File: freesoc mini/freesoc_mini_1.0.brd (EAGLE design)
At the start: 50.8 x 17.8 mm, 50 parts, among them IC1 CY7C68013A-56QFNLFXC, IC2 24LC00OT, Y1 XRCGB24M000F0L00R0

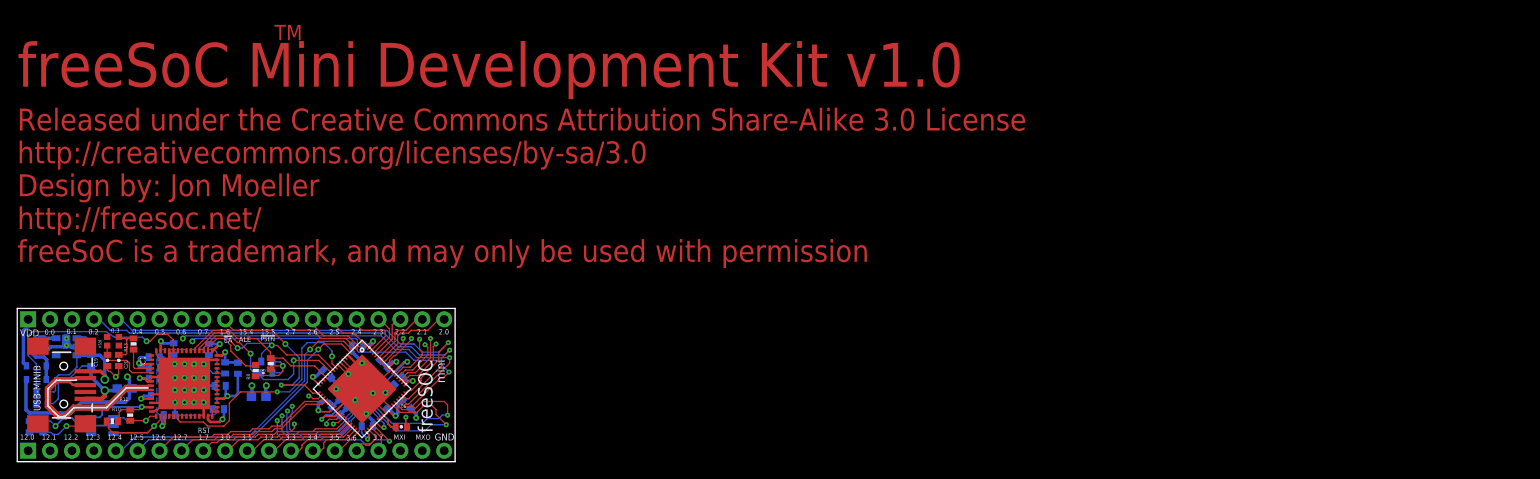
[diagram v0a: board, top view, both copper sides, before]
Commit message: DFM changes to freesoc mini board
All vias tented.

Updated land pattern for FX2 and PSoC for improved reliability and
smaller defect rate.
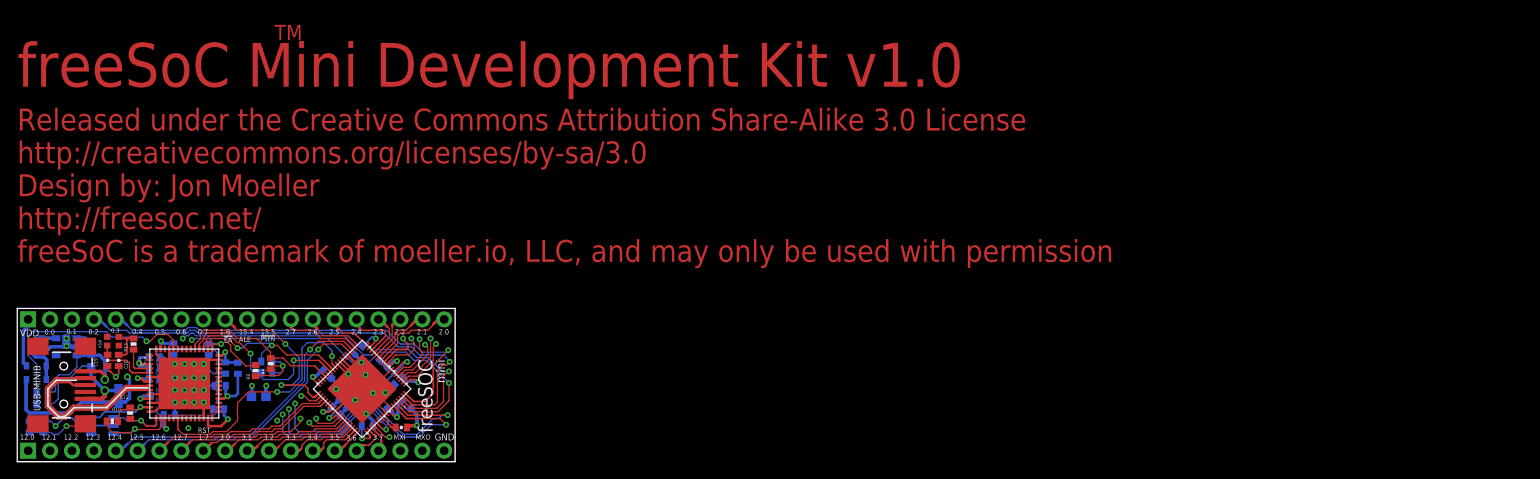
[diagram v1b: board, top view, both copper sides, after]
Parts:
- moved C16 1.13 mm to (17.1, 8.26), turned to 90 degrees
- moved C11 0.53 mm to (45.0, 13.6), turned to 315 degrees
- moved R11 0.24 mm to (18.5, 6.27)
- moved C6 0.08 mm to (50.0, 4.60)
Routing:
- net MXI: track 11.3 -> 18.3 mm
- net MXO: track 15.9 -> 19.0 mm
- net P0.1: track 54.5 -> 57.6 mm
- net P0.0: track 58.0 -> 60.4 mm
- net VCC: track 69.4 -> 71.7 mm
- net VCCD: track 17.2 -> 15.1 mm
- net GND: track 134.2 -> 136.2 mm
- net P0.2: track 51.6 -> 53.7 mm
- net SDA: track 13.3 -> 11.3 mm
- net !PSEN: track 20.2 -> 22.1 mm
- net ALE: track 24.9 -> 26.5 mm
- net !EA: track 20.1 -> 21.5 mm
- net P0.3: track 48.7 -> 50.2 mm
- net P0.7: track 32.7 -> 34.1 mm
- net RESET: track 17.8 -> 19.2 mm
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- added copper zone on layer 15, net N$6
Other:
- board text added: "freeSoC is a trademark of moeller.io, LLC, and may only be used with permission"
- board text removed: "freeSoC is a trademark, and may only be used with permission"

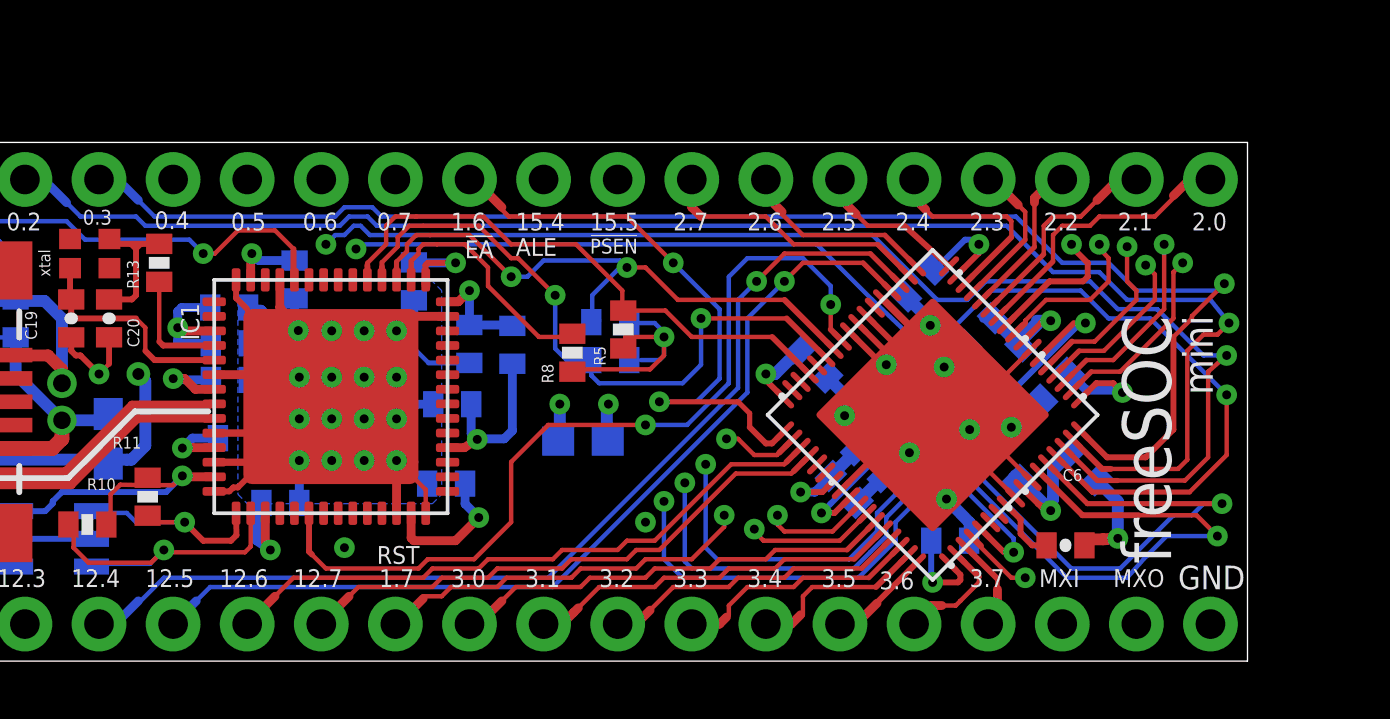
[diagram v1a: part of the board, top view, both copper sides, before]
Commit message: More DFM changes for freesoc mini
Updated FX2 QFN thermal pad to meet cypress spec.

Updated PSoC QFN thermal pad to meet cypress spec.

Added tented vias on thermal pad for both chips, proper solder paste
stencil, and removed solder mask from bottom of vias to prevent
outgassing.
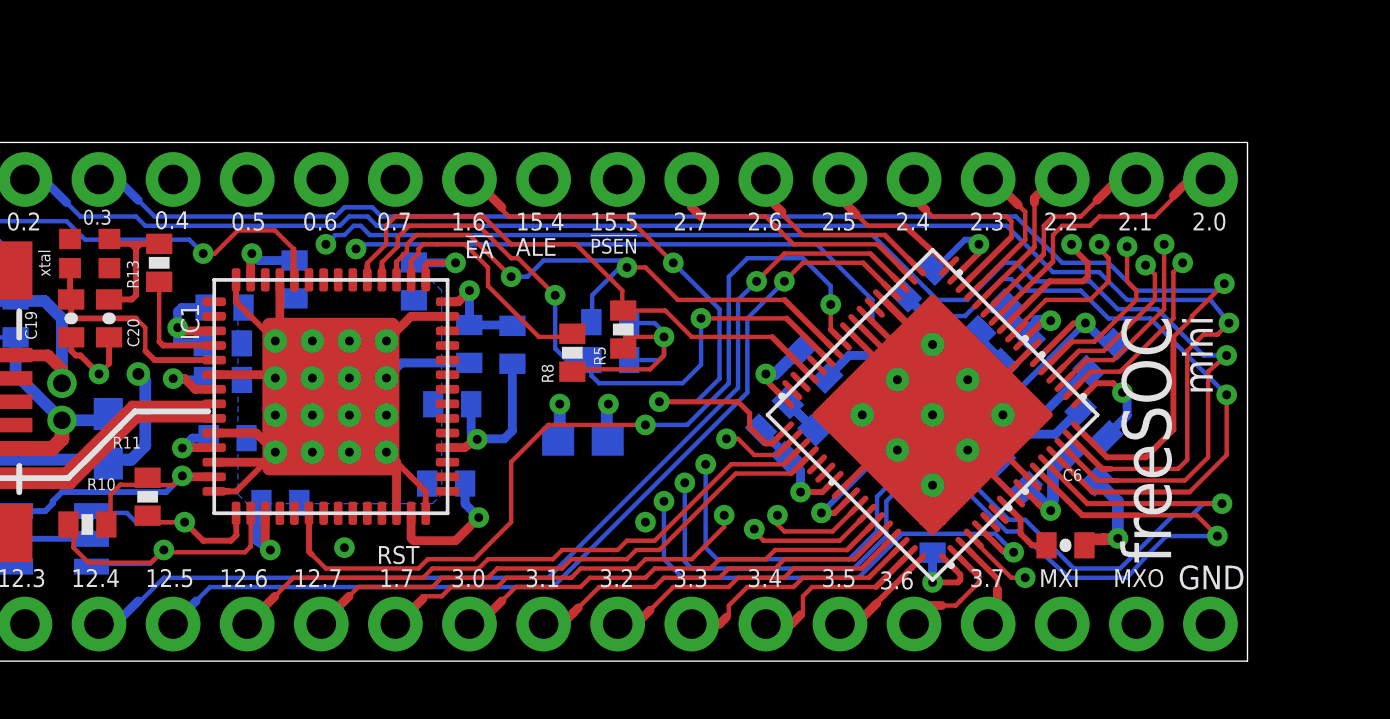
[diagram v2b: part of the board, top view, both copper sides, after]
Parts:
- moved C14 6.57 mm to (51.2, 11.0), turned to 315 degrees
- moved C7 3.64 mm to (40.0, 9.03), turned to 135 degrees
- moved C12 2.17 mm to (40.9, 8.09), turned to 135 degrees
- moved C10 1.82 mm to (50.9, 8.80), turned to 45 degrees
- moved C13 0.67 mm to (47.5, 12.4)
- moved C15 0.65 mm to (45.4, 5.00), turned to 90 degrees
- moved C5 0.45 mm to (48.3, 11.3)
- moved C4 0.40 mm to (48.2, 7.07)
- moved C26 0.32 mm to (21.2, 8.28)
- moved C21 0.24 mm to (21.1, 10.3)
- moved C3 0.24 mm to (21.1, 11.5)
- moved C2 0.16 mm to (21.1, 12.8)
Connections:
- net GND: now also IC1.P$1, IC1.P$10, IC1.P$11, IC1.P$12, IC1.P$13, IC1.P$14, IC1.P$15, IC1.P$16, IC1.P$2, IC1.P$3, IC1.P$4, IC1.P$5, IC1.P$6, IC1.P$7, IC1.P$8, IC1.P$9, U$1.P$1, U$1.P$2, U$1.P$3, U$1.P$4, U$1.P$5, U$1.P$6, U$1.P$7, U$1.P$8, U$1.P$9
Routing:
- net GND: track 136.2 -> 125.2 mm, vias 31 -> 7
- net VDD: track 71.7 -> 68.9 mm
- net P0.0: track 60.4 -> 63.0 mm
- net P1.1: track 48.7 -> 46.4 mm
- net VCCD: track 15.1 -> 17.3 mm
- net VCC: track 71.7 -> 70.7 mm
- net P2.0: track 10.6 -> 11.2 mm
- net P0.1: track 57.6 -> 58.2 mm
